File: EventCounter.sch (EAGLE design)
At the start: 23 parts, among them J1 CONN_42.54_SCREW, Q1 2N7002, Q3 DMG3404, U7 MCP6041, U8 MCP6041

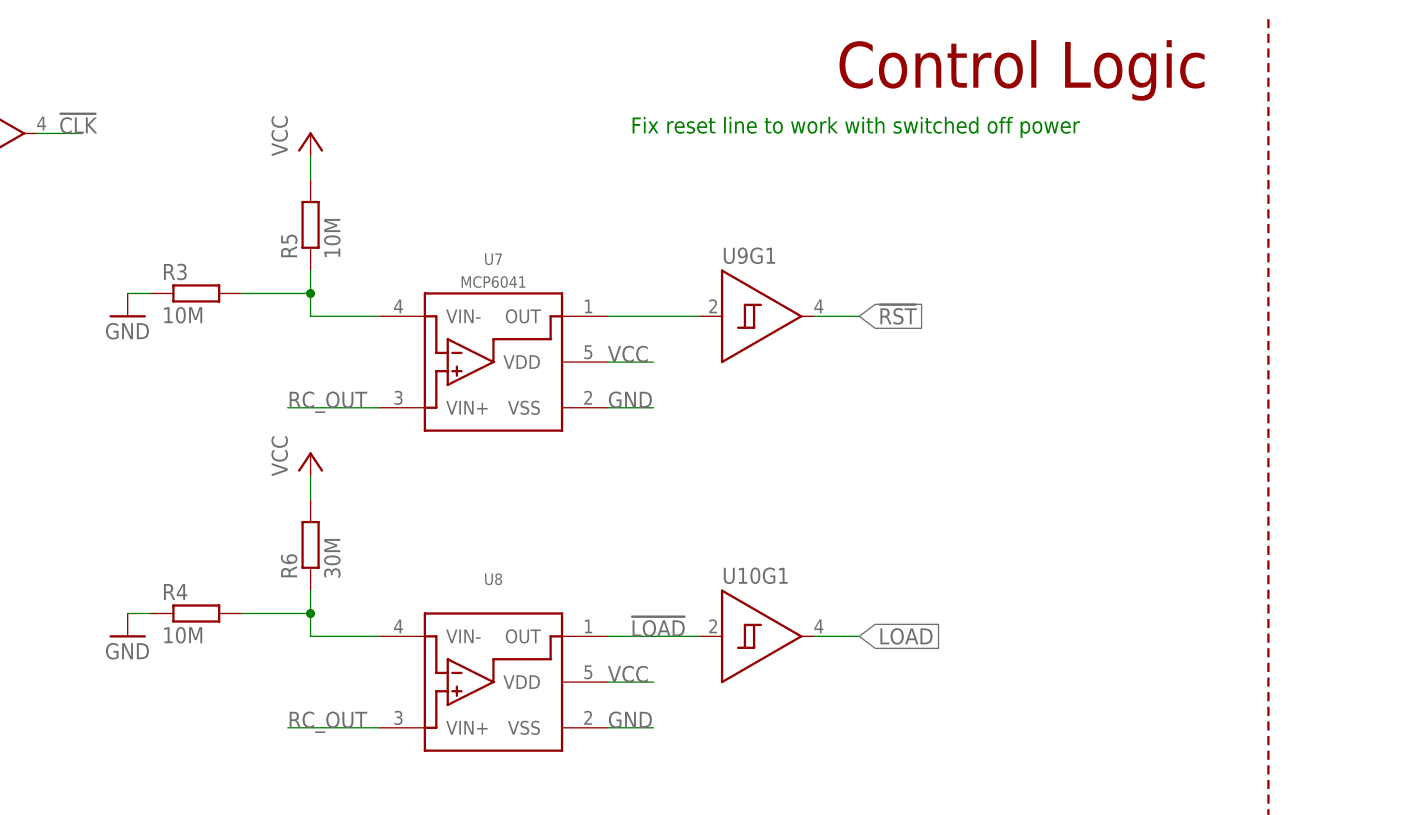
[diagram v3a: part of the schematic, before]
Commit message: Changed resistor divider values for low power
After checking part availability, changed values to more logical ones
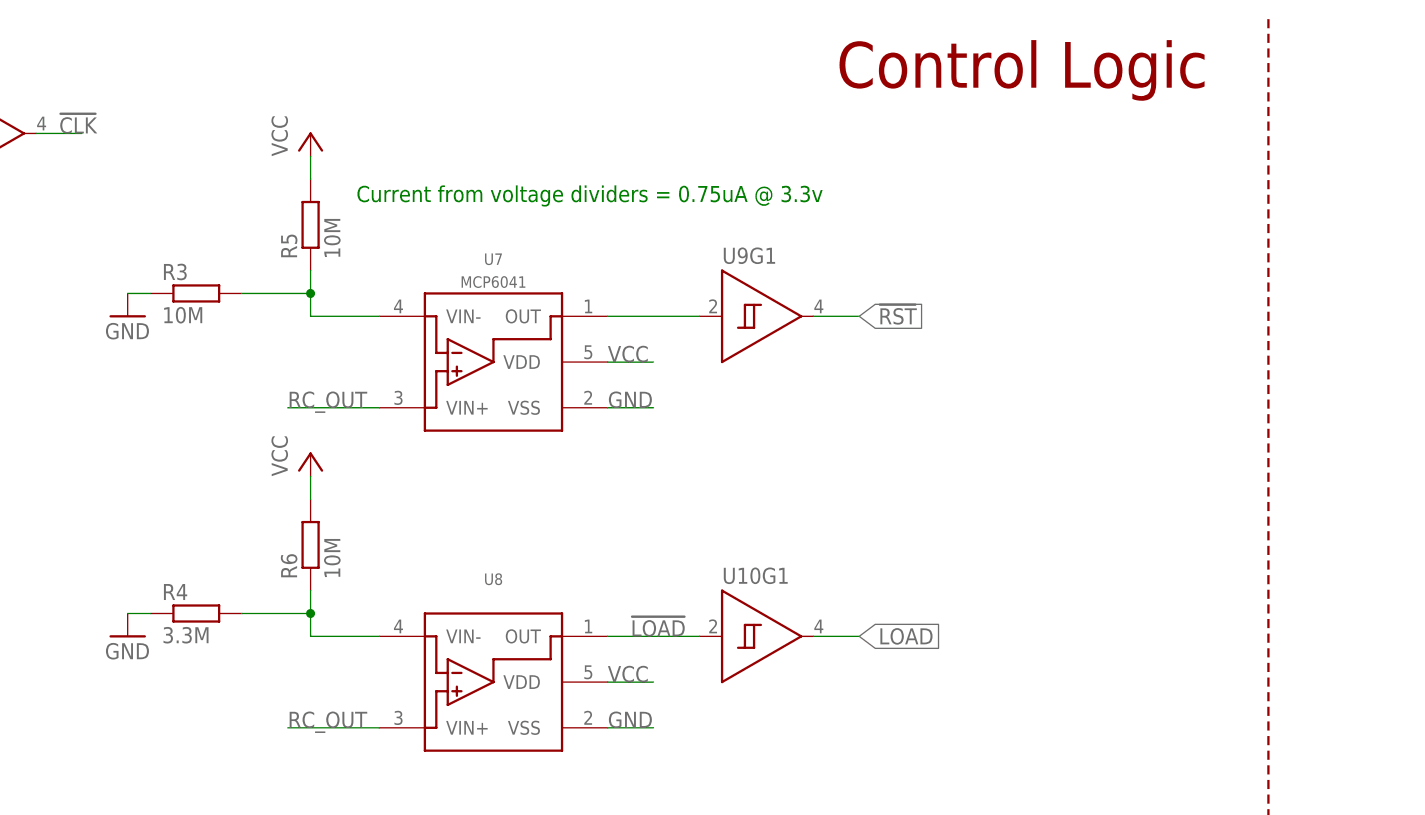
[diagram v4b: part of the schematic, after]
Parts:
- R3: device bschulz_passives:R-EU_10KR0603 -> bschulz_passives:R-EU_10MR0603
- R4: value 10M -> 3.3M; device bschulz_passives:R-EU_10KR0603 -> bschulz_passives:R-EU_3.3MR0603
- R5: device bschulz_passives:R-EU_R0603 -> bschulz_passives:R-EU_10MR0603
- R6: value 30M -> 10M; device bschulz_passives:R-EU_R0603 -> bschulz_passives:R-EU_10MR0603
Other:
- note added: "Current from voltage dividers = 0.75uA @ 3.3v"
- note removed: "Fix reset line to work with switched off power"

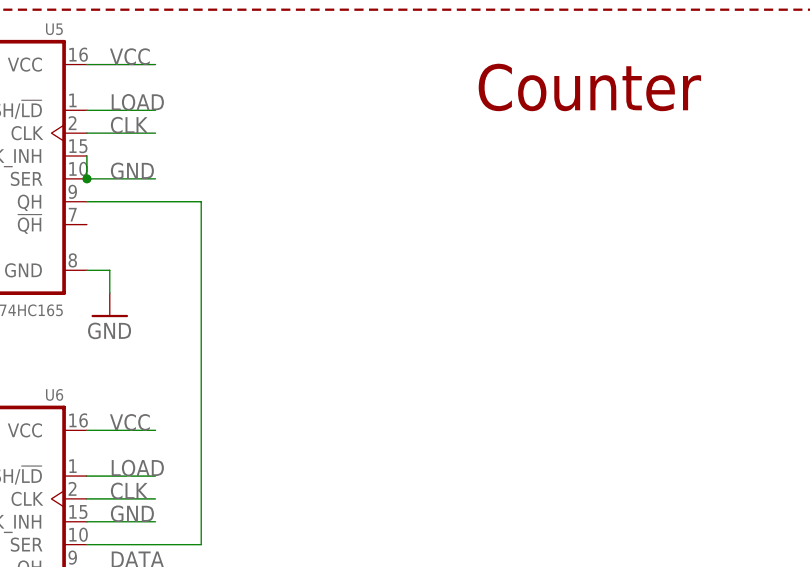
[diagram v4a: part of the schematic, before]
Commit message: Added BOM and decoupling cap
Added BOM files and decoupling capacitor, cleaned up some silkscreen issues, ready for final review
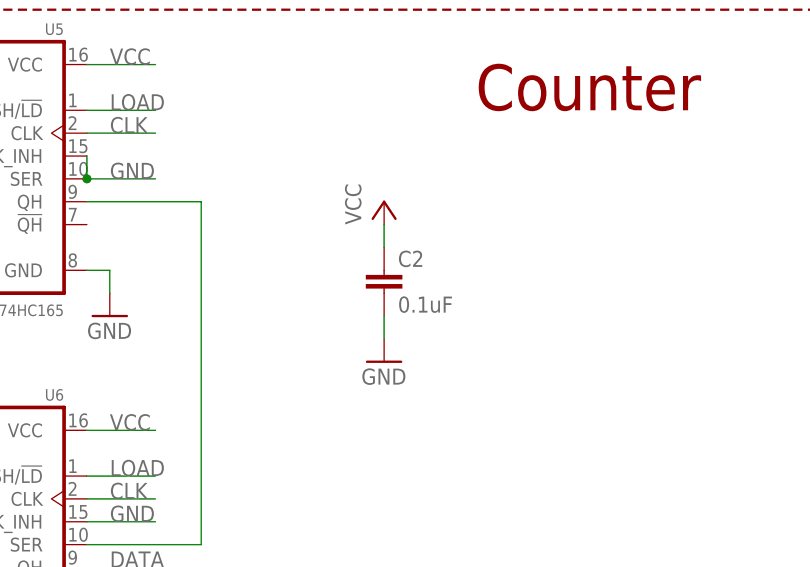
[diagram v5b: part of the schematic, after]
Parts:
- added C2: 0.1uF, bschulz_passives:C-EU0.1UFC0603
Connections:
- net GND: now also C2.2
- net VCC: now also C2.1
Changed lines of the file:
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@@
 <?xml version="1.0" encoding="utf-8"?>
 <!DOCTYPE eagle SYSTEM "eagle.dtd">
-<eagle version="8.5.1">
+<eagle version="9.0.1">
 <drawing>
 <settings>
@@
 <setting verticaltext="up"/>
 </settings>
-<grid distance="0.1" unitdist="inch" unit="mm" style="lines" multiple="1" display="no" altdistance="0.01" altunitdist="inch" altunit="mm"/>
+<grid distance="0.1" unitdist="inch" unit="inch" style="lines" multiple="1" display="no" altdistance="0.01" altunitdist="inch" altunit="inch"/>
 <layers>
 <layer number="1" name="Top" color="4" fill="1" visible="yes" active="no"/>
@@
 <attribute name="REV" value="0.0"/>
 </part>
+<part name="C2" library="bschulz_passives" deviceset="C-EU" device="C0603" technology="0.1UF" value="0.1uF"/>
+<part name="GND10" library="supply1" library_urn="urn:adsk.eagle:library:371" deviceset="GND" device=""/>
+<part name="P+6" library="supply1" library_urn="urn:adsk.eagle:library:371" deviceset="VCC" device=""/>
 </parts>
 <sheets>
@@
 </instance>
 <instance part="FRAME1" gate="G$2" x="172.72" y="0"/>
+<instance part="C2" gate="G$1" x="114.3" y="55.88"/>
+<instance part="GND10" gate="1" x="114.3" y="45.72"/>
+<instance part="P+6" gate="VCC" x="114.3" y="63.5"/>
 </instances>
 <busses>
@@
 <wire x1="231.14" y1="152.4" x2="231.14" y2="154.94" width="0.1524" layer="91"/>
 <pinref part="P+5" gate="VCC" pin="VCC"/>
+</segment>
+<segment>
+<pinref part="C2" gate="G$1" pin="1"/>
+<pinref part="P+6" gate="VCC" pin="VCC"/>
+<wire x1="114.3" y1="58.42" x2="114.3" y2="60.96" width="0.1524" layer="91"/>
 </segment>
 </net>
@@
 <junction x="17.78" y="167.64"/>
 </segment>
+<segment>
+<pinref part="C2" gate="G$1" pin="2"/>
+<pinref part="GND10" gate="1" pin="GND"/>
+<wire x1="114.3" y1="50.8" x2="114.3" y2="48.26" width="0.1524" layer="91"/>
+</segment>
 </net>
